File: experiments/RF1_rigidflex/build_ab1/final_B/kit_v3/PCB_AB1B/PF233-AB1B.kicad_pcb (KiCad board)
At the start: 6 copper layers, 40 x 40 mm, 43 parts, among them J1 RF1 receive-coil flex jumper 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, J2 RF1 rigid-flex hinge exit 12p, SW1 74LVC1G66, SW2 74LVC1G66, U1 OPA2211

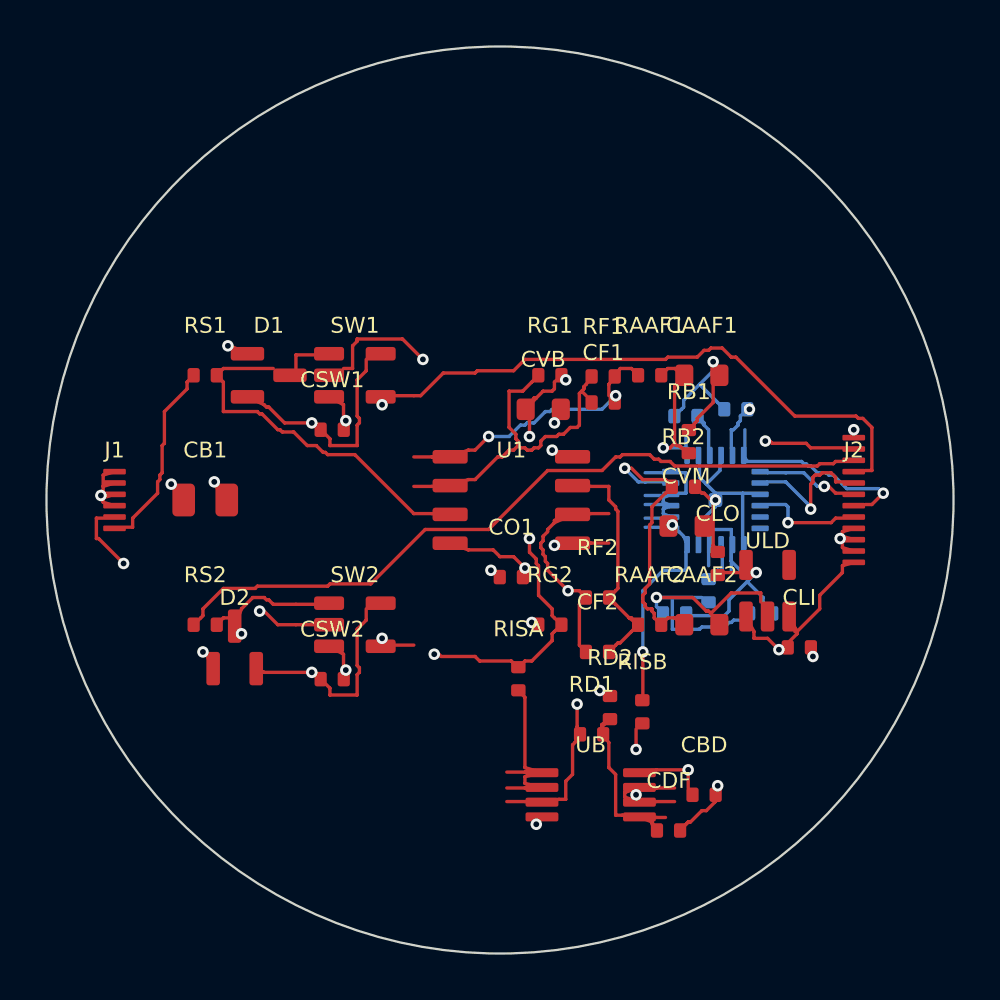
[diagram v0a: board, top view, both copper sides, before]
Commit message: Freerouting as a scripted, checked pipeline step; RF1 AB1A routed to 0 open
- src/pcb/freeroute.py: KiCad board -> Specctra DSN -> Freerouting 2.4.1 (headless,
  pinned jar from Maven Central, SHA-256 checked) -> SES -> KiCad board. Writes the
  repo rules into the net classes (0.15 / 0.16 mm, via 0.508 / 0.254); --hv nets get an
  HV class >= 1.0 mm (rule 6, lower refused); --rip NETS / --strip; JSON report.
- scripts/fetch_freerouting.sh, make freeroute-fetch / freeroute-selftest, bootstrap
  installs Java 25 + the jar (optional, warns); jar is git-ignored.
- tests/freeroute_selftest.py + pipeline step freeroute-selftest + regress rows
  (self-test; RF1 AB1A/AB1B final boards clean, F1 clear). Regress: 122 PASS, 0 FAIL.
- RF1 AB1A: repo router left OUT_GY open; Freerouting (--rip OUT_GY) closed it and
  VBIAS_O. KiCad 9 DRC 0 errors / 0 unconnected, independent DRC 0 fails (min
  clearance 0.165 mm), KiCad Gerbers pass the edge check. AB1B re-exported: still clean.
- RF1 exporter copy: stub test now handles rounded pad corners (CVB.2 was 4 um off
  the copper). Same latent test in the baseline exporter: OPEN_ITEMS 45 (no baseline
  board triggers it).
- finalize_rf1_ab1.sh: optional Freerouting step, KiCad Gerbers, Gerber edge check;
  record_route.py reports the final board's open count; rf1_phase4.py F1 reads the
  final board. PROCESS.md, CLAUDE.md, RF1 README updated.

All results MODELED / tool-checked; no fabricator DRC or CAM review yet.

Co-Authored-By: Claude Opus 5.5 <noreply@anthropic.com>
Claude-Session: https://claude.ai/code/session_01FX4DWSYYjMCFGGA6gmha65
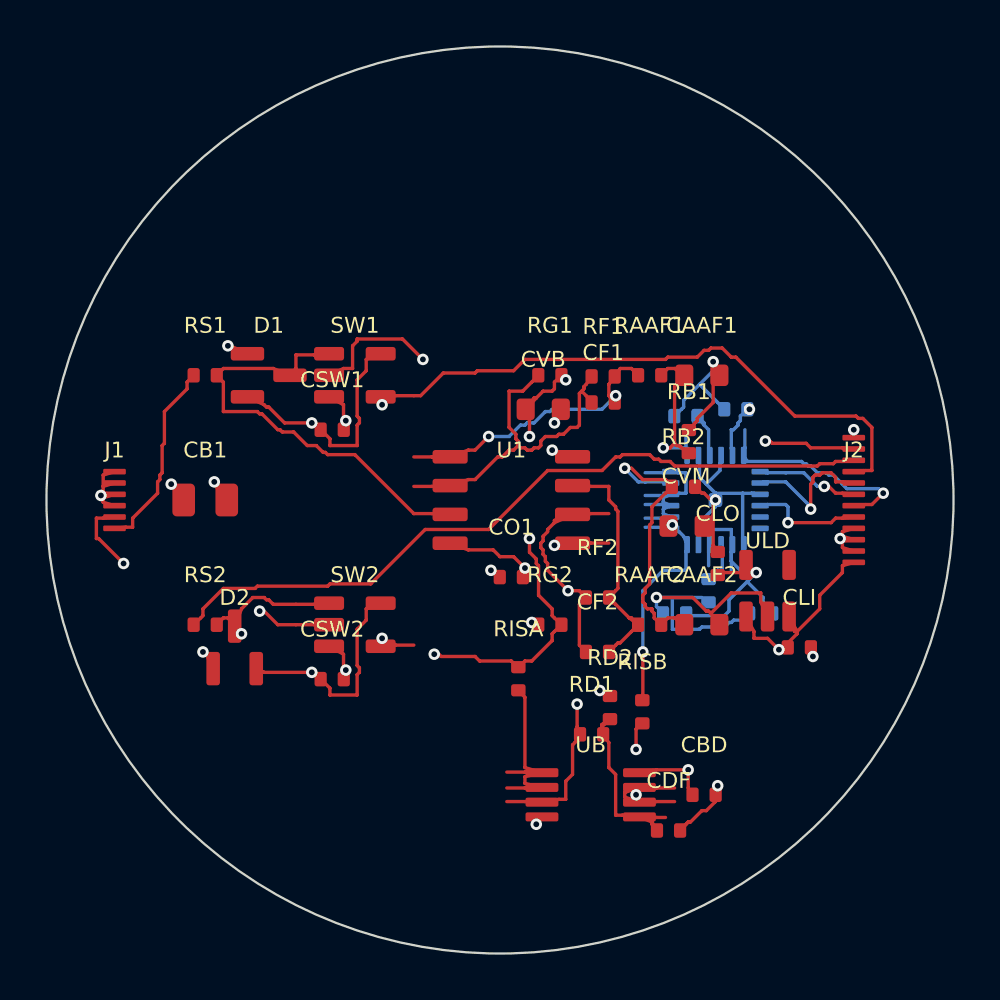
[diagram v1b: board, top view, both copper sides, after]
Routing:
- net GND: track 60.2 -> 67.1 mm
- net +5VA: track 36.9 -> 40.2 mm
- net VCM: track 17.0 -> 20.0 mm
- net VBIAS: track 65.5 -> 67.8 mm
- net IN_Y8: track 17.6 -> 19.5 mm
- net BLANK: track 36.6 -> 38.5 mm
- net +3V3D: track 12.6 -> 13.9 mm
- net IN_MONO: track 22.0 -> 23.1 mm
- net SDO2: track 5.56 -> 6.40 mm
- net SCLK: track 4.12 -> 4.96 mm
- net CS: track 8.69 -> 9.53 mm
- net SDO1: track 3.67 -> 4.51 mm
- net RAW_MONO: track 32.2 -> 32.7 mm
- net RAW_Y8: track 8.11 -> 8.61 mm
